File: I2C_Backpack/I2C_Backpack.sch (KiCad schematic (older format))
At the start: 11 parts, among them P1 CONN_01X04, P2 CONN_01X01, U1 MCP23017_QFN28

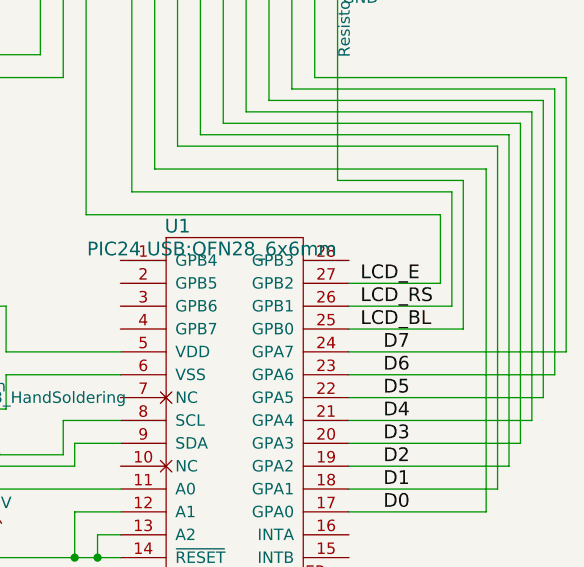
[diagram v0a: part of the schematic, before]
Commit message: Fixed Enable and RS pin mixupt in LCD backpack
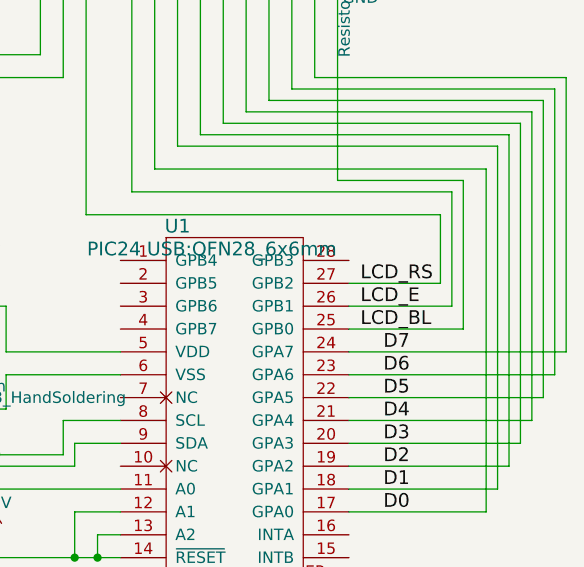
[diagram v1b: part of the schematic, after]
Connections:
- net LCD_E: now also DS1.6 (E), U1.26 (GPB1); no longer DS1.4 (RS), U1.27 (GPB2)
- net LCD_RS: now also DS1.4 (RS), U1.27 (GPB2); no longer DS1.6 (E), U1.26 (GPB1)
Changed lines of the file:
@@
 $EndComp
 Text Label 4500 4950 0    60   ~ 0
+LCD_E
+Text Label 4500 4850 0    60   ~ 0
 LCD_RS
-Text Label 4500 4850 0    60   ~ 0
-LCD_E
 $Comp
 L GND #PWR15
